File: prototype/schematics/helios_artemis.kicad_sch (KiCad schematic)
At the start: 16 parts, among them J1 PV_IN, J2 BAT_OUT

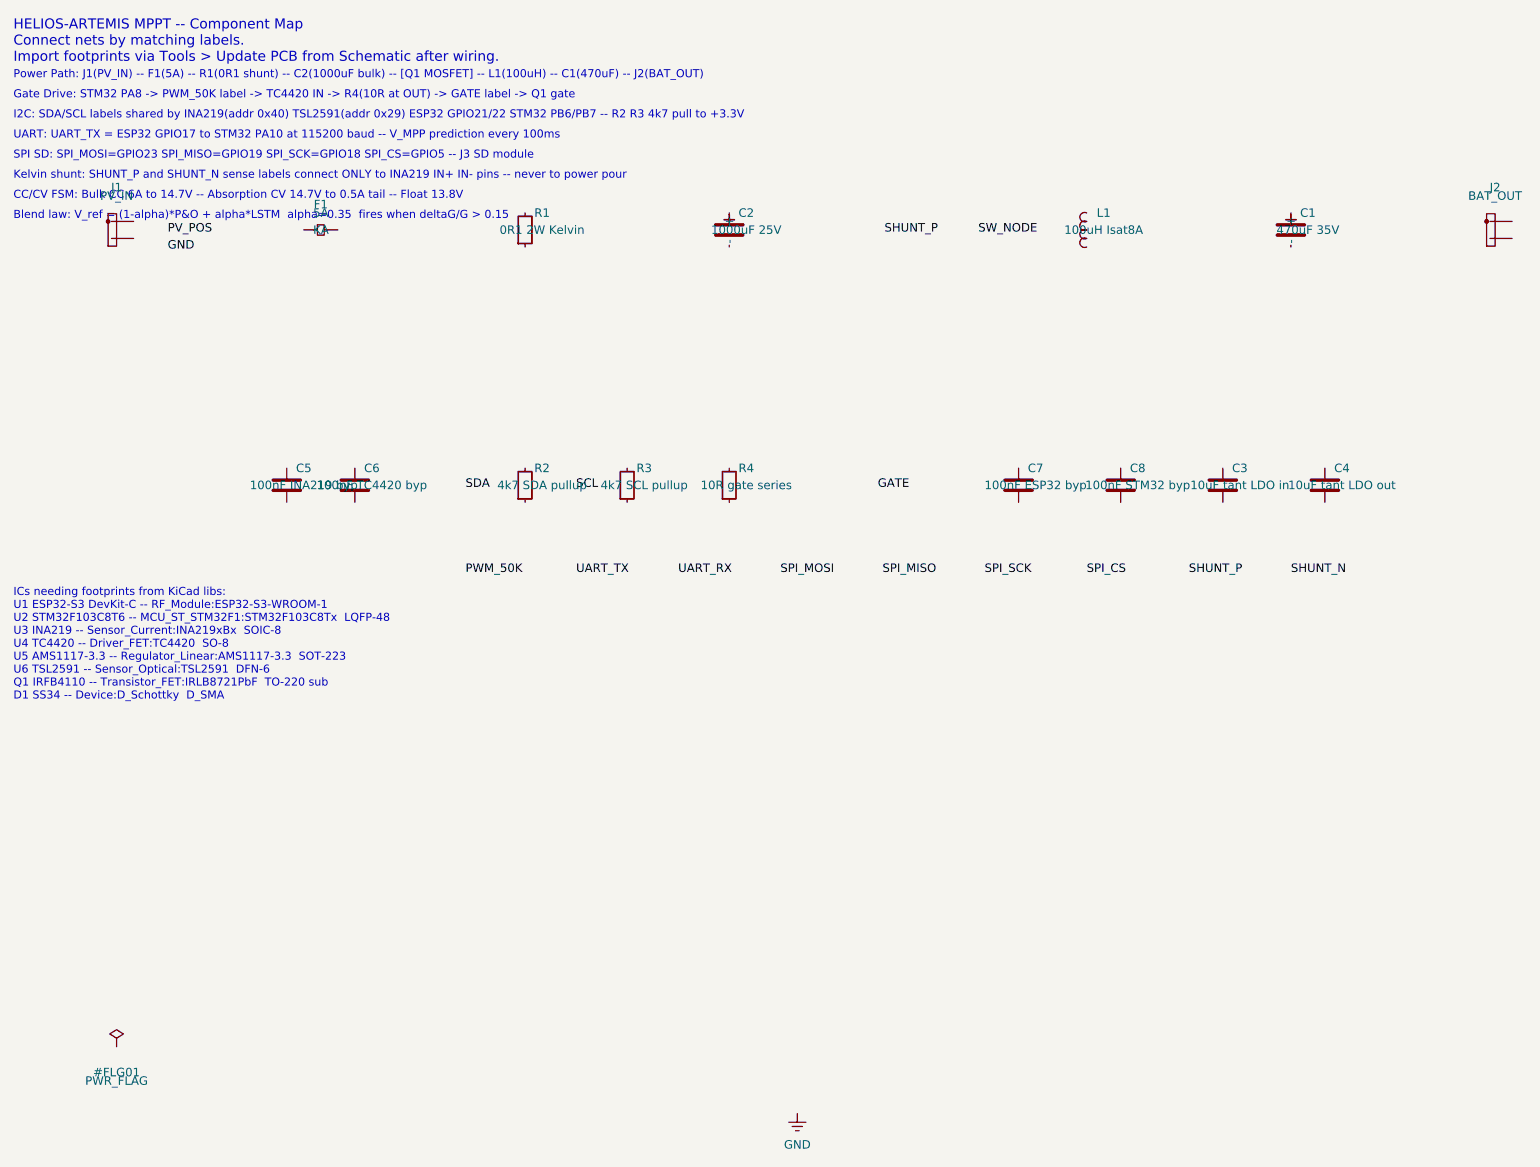
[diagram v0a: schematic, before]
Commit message: Replace TSL2591 sensor with GY302 (BH1750) across firmware, docs, and schematics
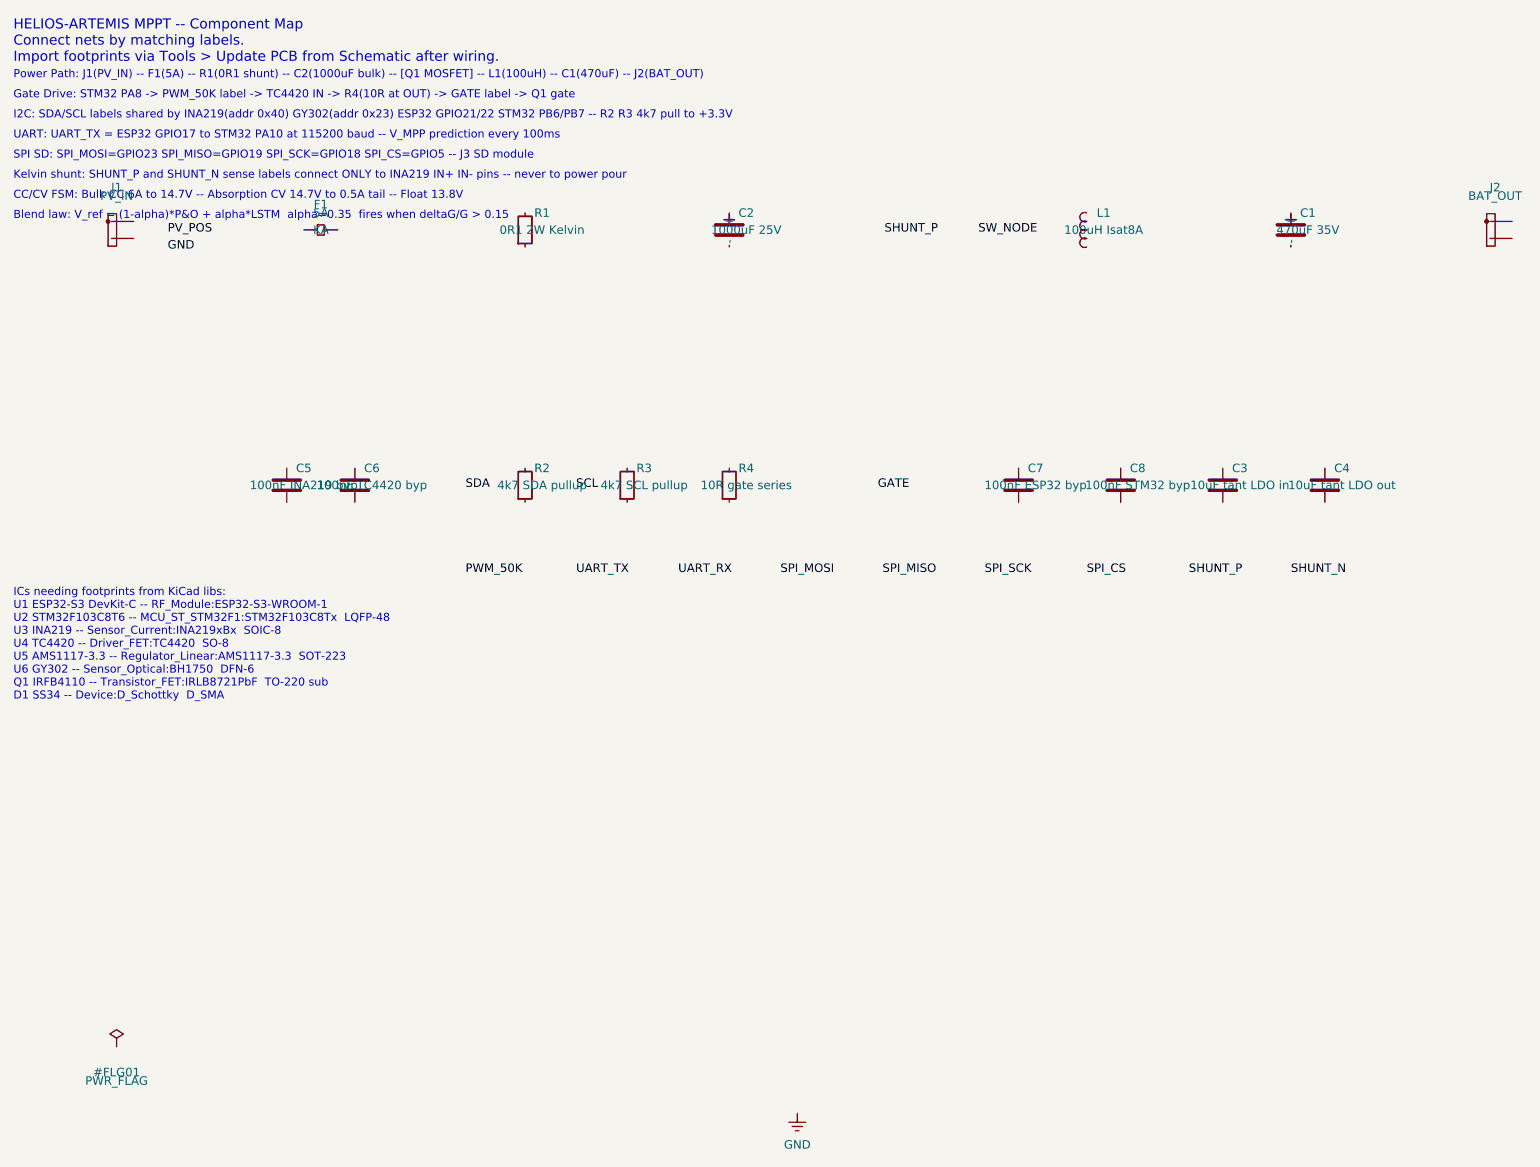
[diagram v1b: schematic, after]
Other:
- note added: "I2C: SDA/SCL labels shared by INA219(addr 0x40) GY302(addr 0x23) ESP32 GPIO21/22 STM32 PB6/PB7 -- R2 R3 4k7 pull to +3.3V"
- note added: "ICs needing footprints from KiCad libs: U1 ESP32-S3 DevKit-C -- RF_Module:ESP32-S3-WROOM-1 U2 STM32F103C8T6 -- MCU_ST_STM32F1:STM32F103C8Tx LQFP-48 U3 INA219 -- Sensor_Current:INA219xBx SOIC-8 U4 TC4420 -- Driver_FET:TC4420 SO-8 U5 AMS1117-3.3 -- Regulator_Linear:AMS1117-3.3 SOT-223 U6 GY302 -- Sensor_Optical:BH1750 DFN-6 Q1 IRFB4110 -- Transistor_FET:IRLB8721PbF TO-220 sub D1 SS34 -- Device:D_Sc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"
- note removed: "I2C: SDA/SCL labels shared by INA219(addr 0x40) TSL2591(addr 0x29) ESP32 GPIO21/22 STM32 PB6/PB7 -- R2 R3 4k7 pull to +3.3V"
- note removed: "ICs needing footprints from KiCad libs: U1 ESP32-S3 DevKit-C -- RF_Module:ESP32-S3-WROOM-1 U2 STM32F103C8T6 -- MCU_ST_STM32F1:STM32F103C8Tx LQFP-48 U3 INA219 -- Sensor_Current:INA219xBx SOIC-8 U4 TC4420 -- Driver_FET:TC4420 SO-8 U5 AMS1117-3.3 -- Regulator_Linear:AMS1117-3.3 SOT-223 U6 TSL2591 -- Sensor_Optical:TSL2591 DFN-6 Q1 IRFB4110 -- Transistor_FET:IRLB8721PbF TO-220 sub D1 SS34 -- Device:D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"
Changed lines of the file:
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@@
     (effects (font (size 1.2 1.2)) (justify left))
   )
-  (text "I2C: SDA/SCL labels shared by INA219(addr 0x40) TSL2591(addr 0x29) ESP32 GPIO21/22 STM32 PB6/PB7 -- R2 R3 4k7 pull to +3.3V"
+  (text "I2C: SDA/SCL labels shared by INA219(addr 0x40) GY302(addr 0x23) ESP32 GPIO21/22 STM32 PB6/PB7 -- R2 R3 4k7 pull to +3.3V"
     (at 10 21 0)
     (effects (font (size 1.2 1.2)) (justify left))
@@
     (effects (font (size 1.2 1.2)) (justify left))
   )
-  (text "ICs needing footprints from KiCad libs:\nU1 ESP32-S3 DevKit-C -- RF_Module:ESP32-S3-WROOM-1\nU2 STM32F103C8T6 -- MCU_ST_STM32F1:STM32F103C8Tx  LQFP-48\nU3 INA219 -- Sensor_Current:INA219xBx  SOIC-8\nU4 TC4420 -- Driver_FET:TC4420  SO-8\nU5 AMS1117-3.3 -- Regulator_Linear:AMS1117-3.3  SOT-223\nU6 TSL2591 -- Sensor_Optical:TSL2591  DFN-6\nQ1 IRFB4110 -- Transistor_FET:IRLB8721PbF  TO-220 sub\nD1 SS34 -- Device:D_Schottky  D_SMA"
+  (text "ICs needing footprints from KiCad libs:\nU1 ESP32-S3 DevKit-C -- RF_Module:ESP32-S3-WROOM-1\nU2 STM32F103C8T6 -- MCU_ST_STM32F1:STM32F103C8Tx  LQFP-48\nU3 INA219 -- Sensor_Current:INA219xBx  SOIC-8\nU4 TC4420 -- Driver_FET:TC4420  SO-8\nU5 AMS1117-3.3 -- Regulator_Linear:AMS1117-3.3  SOT-223\nU6 GY302 -- Sensor_Optical:BH1750  DFN-6\nQ1 IRFB4110 -- Transistor_FET:IRLB8721PbF  TO-220 sub\nD1 SS34 -- Device:D_Schottky  D_SMA"
     (at 10 100 0)
     (effects (font (size 1.2 1.2)) (justify left))
